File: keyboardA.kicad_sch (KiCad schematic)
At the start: 0 parts

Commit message: creted most of the schematic
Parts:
- added C1: 4.7uF, symbol Device:C
- added C2, C4, C5: 0.1uF, symbol Device:C
- added C3, C6, C7: 1uF, symbol Device:C
- added F1: 1A, symbol Device:Polyfuse
- added J1: USB_C_Receptacle_USB2.0_16P, symbol Connector:USB_C_Receptacle_USB2.0_16P
- added R1: 10k, symbol Device:R
- added R2, R3: 5.1k, symbol Device:R
- added SW1: SW_Push, symbol Switch:SW_Push
- added SW2: SW_SPDT, symbol Switch:SW_SPDT
- added U1: STM32G0B1CBTx, Package_QFP:LQFP-48_7x7mm_P0.5mm, symbol MCU_ST_STM32G0:STM32G0B1CBTx
- added U2: SRV05-4, Package_TO_SOT_SMD:SOT-23-6, symbol Power_Protection:SRV05-4
- added U3: XC6206P332MR, Package_TO_SOT_SMD:SOT-23-3, symbol Regulator_Linear:XC6206PxxxMR
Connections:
- new net: J1.A5 (CC1), R3.1
- new net: J1.B5 (CC2), R2.1
- new net: R1.2, SW2.2 (B)
- new net +3.3V: C1.1, C2.1, C3.1, C4.1, C7.1, SW2.3 (C), U1.4 (VBAT), U1.5 (VREF+), U1.6 (VDD), U3.2 (VO)
- new net +5V: C6.1, F1.2, U2.5 (VP), U3.3 (VI)
- new net BOOT0: R1.1, U1.36 (PA14)
- new net D+: J1.A6 (D+), J1.B6 (D+), U1.34 (PA10/PA12)
- new net D-: J1.A7 (D-), J1.B7 (D-), U1.33 (PA9/PA11)
- new net GND: C1.2, C2.2, C3.2, C4.2, C5.2, C6.2, C7.2, J1.A1 (GND), J1.A12 (GND), J1.B1 (GND), J1.B12 (GND), J1.SH (SHIELD), R2.2, R3.2, SW1.2, SW2.1 (A), U1.7 (VSS), U2.2 (VN), U3.1 (GND)
- new net VBUS: F1.1, J1.A4 (VBUS), J1.A9 (VBUS), J1.B4 (VBUS), J1.B9 (VBUS)
- new net nRST: C5.1, SW1.1, U1.10 (PF2)
- no-connect marks 0 -> 2
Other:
- added sheet Switch Matrix (matrix.kicad_sch)

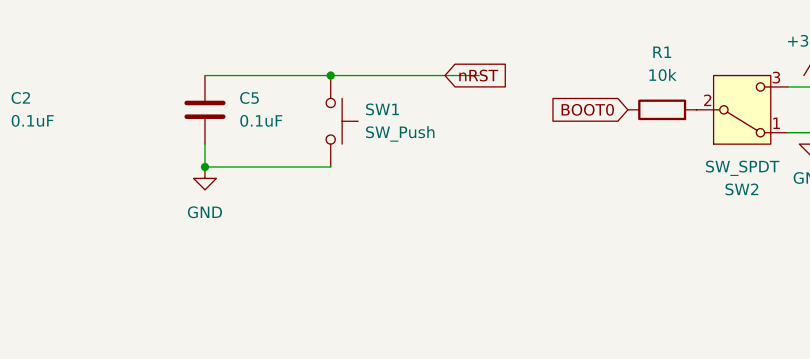
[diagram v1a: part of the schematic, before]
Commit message: added a keyswitch submodule
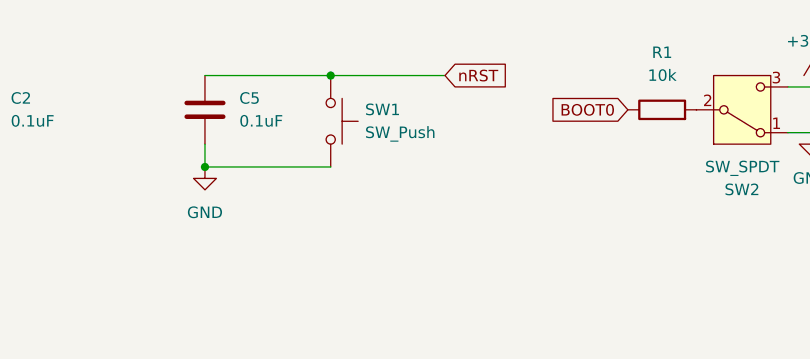
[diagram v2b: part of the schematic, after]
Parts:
- C1, C2, C3, C4, C5, C6, C7: footprint (none) -> Capacitor_SMD:C_0805_2012Metric
- F1: footprint (none) -> Fuse:Fuse_1206_3216Metric
- J1: footprint (none) -> Connector_USB:USB_C_Receptacle_HRO_TYPE-C-31-M-12
- R1, R2, R3: footprint (none) -> Resistor_SMD:R_0805_2012Metric
- SW1: footprint (none) -> Button_Switch_SMD:SW_SPST_TS-1088-xR020
- SW2: footprint (none) -> Button_Switch_SMD:SW_SPDT_PCM12
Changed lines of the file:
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@@
 	(wire
 		(pts
-			(xy 148.59 21.59) (xy 165.1 21.59)
+			(xy 148.59 21.59) (xy 161.29 21.59)
 		)
 		(stroke
@@
 			)
 		)
-		(property "Footprint" ""
+		(property "Footprint" "Capacitor_SMD:C_0805_2012Metric"
 			(at 211.7852 130.81 0)
 			(hide yes)
@@
 			)
 		)
-		(property "Footprint" ""
+		(property "Footprint" "Capacitor_SMD:C_0805_2012Metric"
 			(at 94.9452 29.21 0)
 			(hide yes)
@@
 			)
 		)
-		(property "Footprint" ""
+		(property "Footprint" "Button_Switch_SMD:SW_SPST_TS-1088-xR020"
 			(at 153.67 26.67 0)
 			(hide yes)
@@
 			)
 		)
-		(property "Footprint" ""
+		(property "Footprint" "Capacitor_SMD:C_0805_2012Metric"
 			(at 135.5852 29.21 0)
 			(hide yes)
@@
 			)
 		)
-		(property "Footprint" ""
+		(property "Footprint" "Resistor_SMD:R_0805_2012Metric"
 			(at 267.462 40.64 90)
 			(hide yes)
@@
 			)
 		)
-		(property "Footprint" ""
+		(property "Footprint" "Fuse:Fuse_1206_3216Metric"
 			(at 264.16 22.86 0)
 			(hide yes)
@@
 			)
 		)
-		(property "Footprint" ""
+		(property "Footprint" "Capacitor_SMD:C_0805_2012Metric"
 			(at 244.8052 130.81 0)
 			(hide yes)
@@
 			)
 		)
-		(property "Footprint" ""
+		(property "Footprint" "Connector_USB:USB_C_Receptacle_HRO_TYPE-C-31-M-12"
 			(at 231.14 39.37 0)
 			(hide yes)
@@
 			)
 		)
-		(property "Footprint" ""
+		(property "Footprint" "Capacitor_SMD:C_0805_2012Metric"
 			(at 46.6852 29.21 0)
 			(hide yes)
@@
 			)
 		)
-		(property "Footprint" ""
+		(property "Footprint" "Button_Switch_SMD:SW_SPDT_PCM12"
 			(at 194.31 25.4 0)
 			(hide yes)
@@
 			)
 		)
-		(property "Footprint" ""
+		(property "Footprint" "Capacitor_SMD:C_0805_2012Metric"
 			(at 31.4452 29.21 0)
 			(hide yes)
@@
 			)
 		)
-		(property "Footprint" ""
+		(property "Footprint" "Resistor_SMD:R_0805_2012Metric"
 			(at 257.302 40.64 90)
 			(hide yes)
@@
 			)
 		)
-		(property "Footprint" ""
+		(property "Footprint" "Capacitor_SMD:C_0805_2012Metric"
 			(at 110.1852 29.21 0)
 			(hide yes)
@@
 			)
 		)
-		(property "Footprint" ""
+		(property "Footprint" "Resistor_SMD:R_0805_2012Metric"
 			(at 185.42 27.178 90)
 			(hide yes)

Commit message: finished assigning footprints
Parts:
- C1, C2, C3, C4, C5, C6, C7: footprint Capacitor_SMD:C_0805_2012Metric -> Capacitor_SMD:C_0805_2012Metric_Pad1.18x1.45mm_HandSolder
- R1, R2, R3: footprint Resistor_SMD:R_0805_2012Metric -> Resistor_SMD:R_0805_2012Metric_Pad1.20x1.40mm_HandSolder
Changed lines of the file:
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@@
 			)
 		)
-		(property "Footprint" "Capacitor_SMD:C_0805_2012Metric"
+		(property "Footprint" "Capacitor_SMD:C_0805_2012Metric_Pad1.18x1.45mm_HandSolder"
 			(at 211.7852 130.81 0)
 			(hide yes)
@@
 			)
 		)
-		(property "Footprint" "Capacitor_SMD:C_0805_2012Metric"
+		(property "Footprint" "Capacitor_SMD:C_0805_2012Metric_Pad1.18x1.45mm_HandSolder"
 			(at 94.9452 29.21 0)
 			(hide yes)
@@
 			)
 		)
-		(property "Footprint" "Capacitor_SMD:C_0805_2012Metric"
+		(property "Footprint" "Capacitor_SMD:C_0805_2012Metric_Pad1.18x1.45mm_HandSolder"
 			(at 135.5852 29.21 0)
 			(hide yes)
@@
 			)
 		)
-		(property "Footprint" "Resistor_SMD:R_0805_2012Metric"
+		(property "Footprint" "Resistor_SMD:R_0805_2012Metric_Pad1.20x1.40mm_HandSolder"
 			(at 267.462 40.64 90)
 			(hide yes)
@@
 			)
 		)
-		(property "Footprint" "Capacitor_SMD:C_0805_2012Metric"
+		(property "Footprint" "Capacitor_SMD:C_0805_2012Metric_Pad1.18x1.45mm_HandSolder"
 			(at 244.8052 130.81 0)
 			(hide yes)
@@
 			)
 		)
-		(property "Footprint" "Capacitor_SMD:C_0805_2012Metric"
+		(property "Footprint" "Capacitor_SMD:C_0805_2012Metric_Pad1.18x1.45mm_HandSolder"
 			(at 46.6852 29.21 0)
 			(hide yes)
@@
 			)
 		)
-		(property "Footprint" "Capacitor_SMD:C_0805_2012Metric"
+		(property "Footprint" "Capacitor_SMD:C_0805_2012Metric_Pad1.18x1.45mm_HandSolder"
 			(at 31.4452 29.21 0)
 			(hide yes)
@@
 			)
 		)
-		(property "Footprint" "Resistor_SMD:R_0805_2012Metric"
+		(property "Footprint" "Resistor_SMD:R_0805_2012Metric_Pad1.20x1.40mm_HandSolder"
 			(at 257.302 40.64 90)
 			(hide yes)
@@
 			)
 		)
-		(property "Footprint" "Capacitor_SMD:C_0805_2012Metric"
+		(property "Footprint" "Capacitor_SMD:C_0805_2012Metric_Pad1.18x1.45mm_HandSolder"
 			(at 110.1852 29.21 0)
 			(hide yes)
@@
 			)
 		)
-		(property "Footprint" "Resistor_SMD:R_0805_2012Metric"
+		(property "Footprint" "Resistor_SMD:R_0805_2012Metric_Pad1.20x1.40mm_HandSolder"
 			(at 185.42 27.178 90)
 			(hide yes)

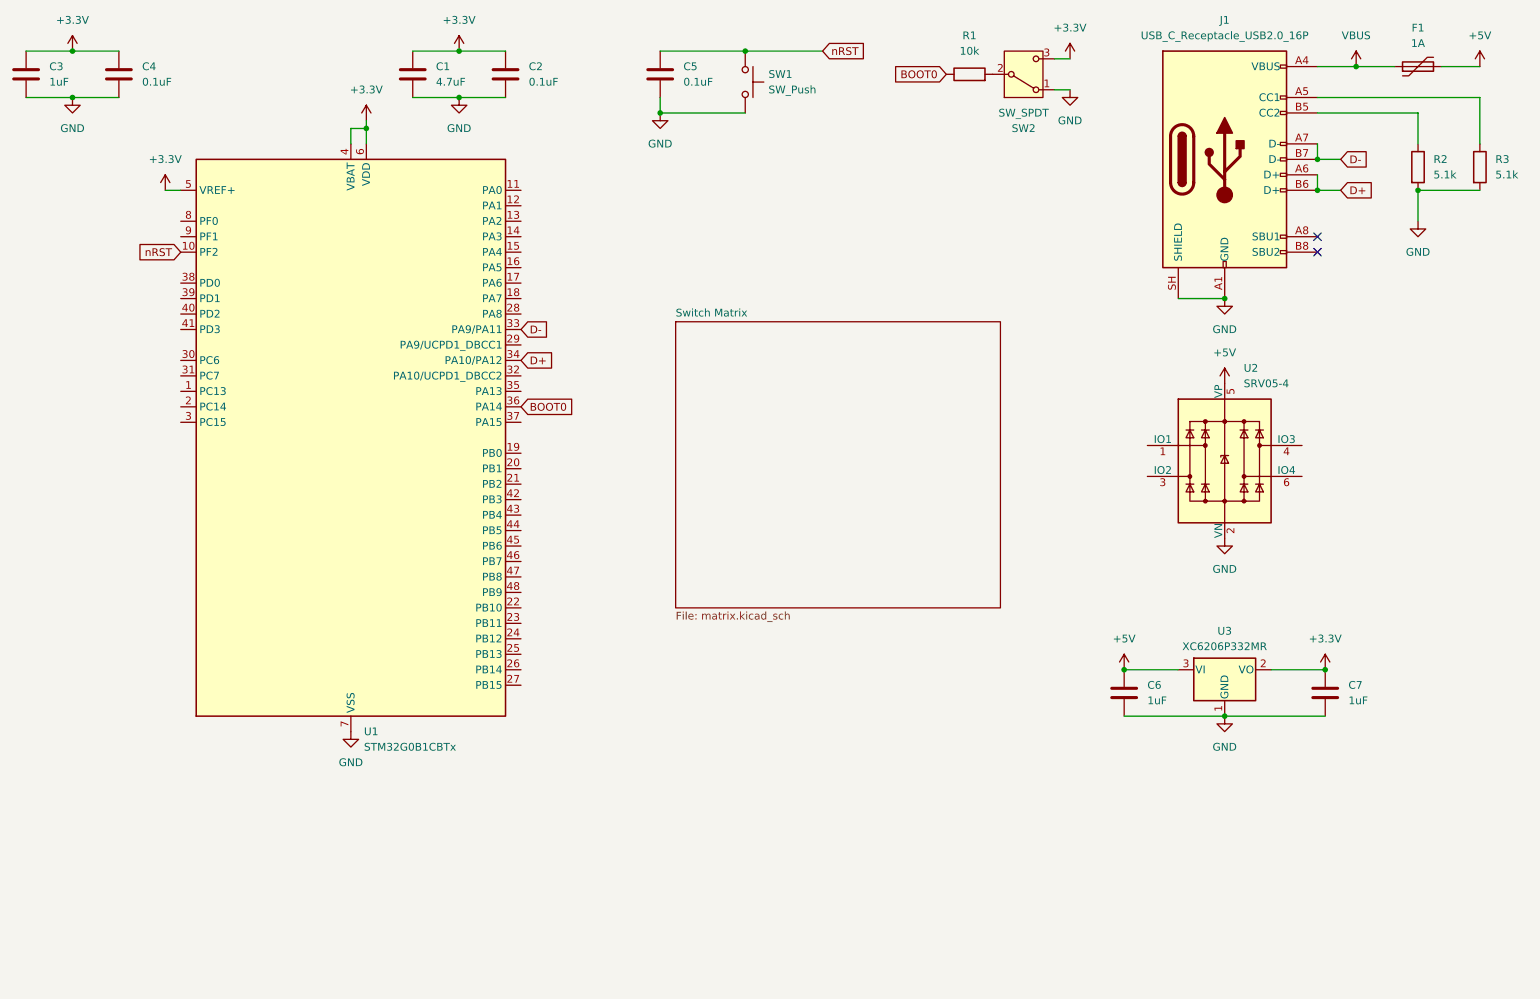
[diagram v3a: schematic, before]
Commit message: thought i was done with pcb but forgot to add a second usb port
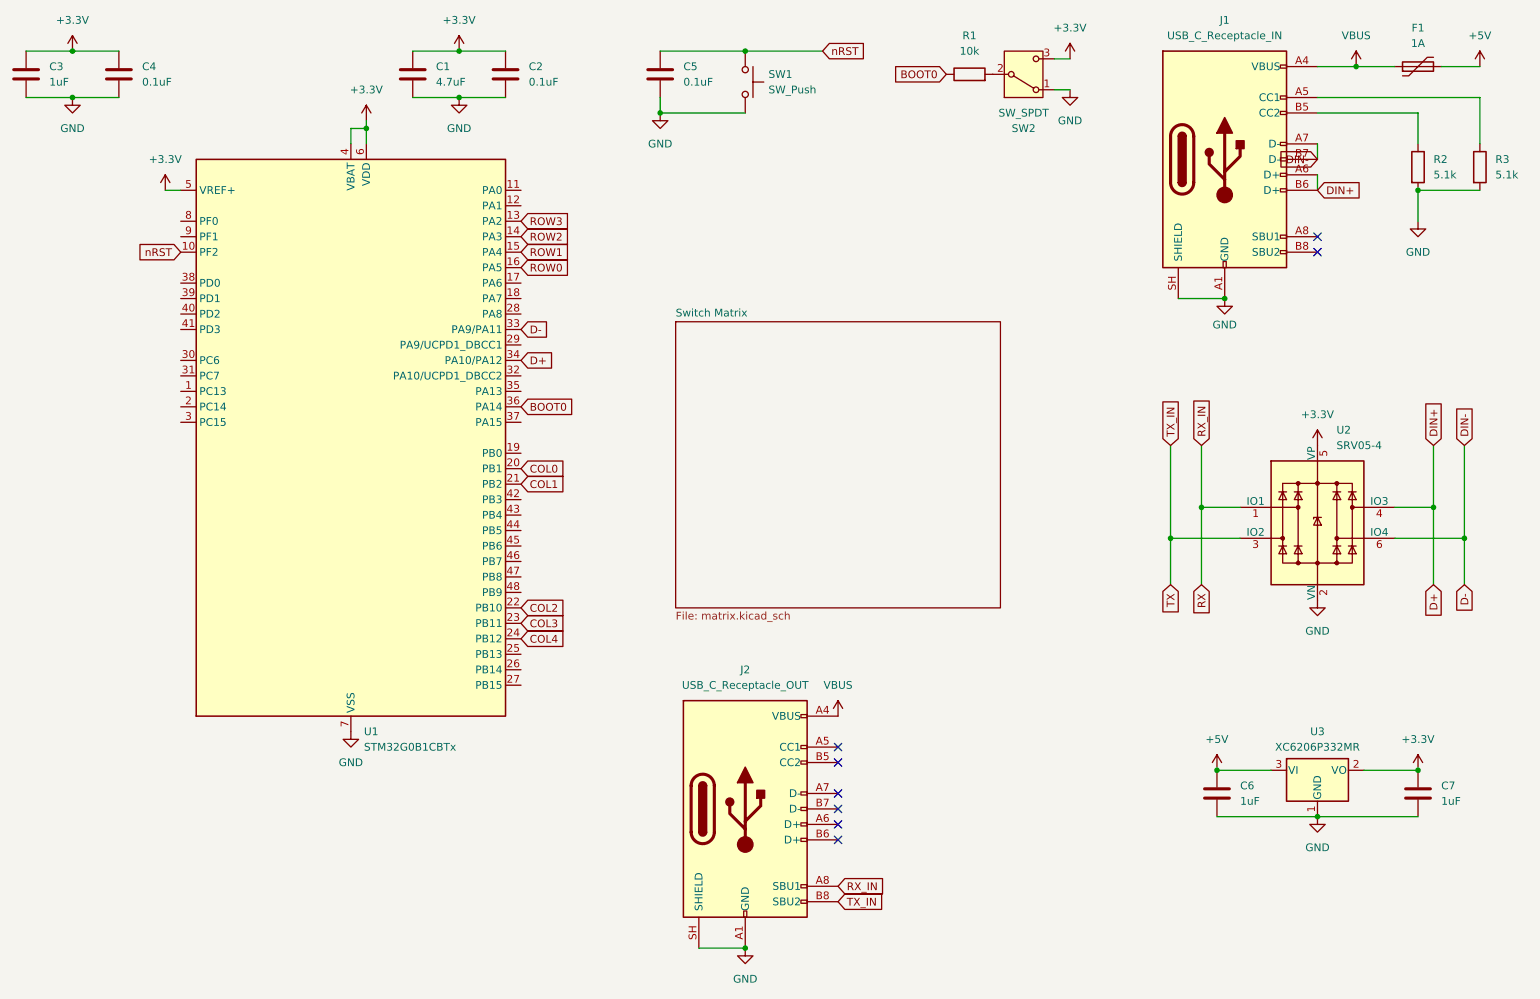
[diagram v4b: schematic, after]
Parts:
- added J2: USB_C_Receptacle_OUT, Connector_USB:USB_C_Receptacle_HRO_TYPE-C-31-M-12, symbol Connector:USB_C_Receptacle_USB2.0_16P
- J1: value USB_C_Receptacle_USB2.0_16P -> USB_C_Receptacle_IN
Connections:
- net +3.3V: now also U2.5 (VP)
- net +5V: no longer U2.5 (VP)
- net D+: now also U2.4 (IO3)
- net D-: now also U2.6 (IO4)
- net GND: now also J2.A1 (GND), J2.A12 (GND), J2.B1 (GND), J2.B12 (GND), J2.SH (SHIELD)
- net VBUS: now also J2.A4 (VBUS), J2.A9 (VBUS), J2.B4 (VBUS), J2.B9 (VBUS)
- net ROW3: now reaches U1.13 (PA2)
- net ROW2: now reaches U1.14 (PA3)
- net ROW1: now reaches U1.15 (PA4)
- net ROW0: now reaches U1.16 (PA5)
- net COL0: now reaches U1.20 (PB1)
- net COL1: now reaches U1.21 (PB2)
- net COL2: now reaches U1.22 (PB10)
- net COL3: now reaches U1.23 (PB11)
- net COL4: now reaches U1.24 (PB12)
- net RX: now reaches U2.1 (IO1)
- net RX: now also J2.A8 (SBU1)
- net TX: now reaches U2.3 (IO2)
- net TX: now also J2.B8 (SBU2)
- no-connect marks 2 -> 8
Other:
- moved on the sheet: C6, C7, U2, U3
